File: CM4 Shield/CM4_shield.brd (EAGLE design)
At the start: 191.8 x 123.4 mm, 40 parts, among them J1 TERMINALBLOCK/TOYO/2PIN/5MMPI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, J3 RASPBERRYPI-40-PIN-GPIO_PTH_N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, X4 DOOR LOCK, X6 TOWER LIGHT

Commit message: Design updates
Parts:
- moved TP18 7.55 mm to (112.4, 5.84)
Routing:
- net DOOR_FEEDBACK: track 79.6 -> 81.5 mm
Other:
- board text added: "24V"
- board text added: "DOOR FEEDBACK"
- board text added: "DOOR LOCK"
- board text added: "GND"
- board text added: "MF_DOOR"
- board text added: "MF_TWRL_G"
- board text added: "MF_TWRL_R"
- board text added: "MF_TWRL_Y"
- board text added: "TWR_G"
- board text added: "TWR_R"
- board text added: "TWR_Y"
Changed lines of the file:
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@@
 <wire x1="90.932" y1="61.468" x2="28.194" y2="55.626" width="0.001" layer="51"/>
 <wire x1="27.94" y1="61.214" x2="90.932" y2="55.626" width="0.001" layer="51"/>
-<text x="111.387" y="-1.656" size="1.016" layer="21">24V INPUT</text>
+<text x="113.927" y="2.662" size="1.016" layer="21">24V INPUT</text>
 <text x="67.818" y="41.529" size="1.016" layer="21" rot="R180">5V DISPLAY</text>
 <wire x1="131" y1="-6" x2="131" y2="0" width="0.0762" layer="51"/>
@@
 <wire x1="113.792" y1="13.716" x2="110.49" y2="17.018" width="0.1524" layer="20" curve="90"/>
 <wire x1="110.49" y1="17.018" x2="106.934" y2="17.018" width="0.1524" layer="20"/>
+<text x="108.458" y="-10.16" size="0.6096" layer="27">GND</text>
+<text x="99.822" y="-0.508" size="0.6096" layer="27" rot="R90">GND</text>
+<text x="124.968" y="-4.318" size="0.6096" layer="27" rot="R180">GND</text>
+<text x="105.41" y="29.21" size="0.3048" layer="27" rot="R180">DOOR LOCK</text>
+<text x="112.268" y="3.81" size="0.6096" layer="27">24V</text>
+<text x="114.554" y="2.032" size="0.6096" layer="27">24V</text>
+<text x="119.38" y="2.032" size="0.6096" layer="27">GND</text>
+<text x="119.634" y="30.226" size="0.4064" layer="27">TWR_R</text>
+<text x="121.412" y="8.382" size="0.4064" layer="27" rot="R270">TWR_G</text>
+<text x="120.65" y="42.418" size="0.4064" layer="27">TWR_Y</text>
+<text x="110.236" y="39.116" size="0.4064" layer="27">MF_DOOR</text>
+<text x="99.314" y="-10.16" size="0.3048" layer="27">MF_TWRL_R</text>
+<text x="102.616" y="-10.16" size="0.3048" layer="27">MF_TWRL_Y</text>
+<text x="105.41" y="-10.16" size="0.3048" layer="27">MF_TWRL_G</text>
+<text x="110.744" y="6.604" size="0.3048" layer="27">DOOR FEEDBACK</text>
 </plain>
 <attributes>
@@
 <element name="TP16" library="SparkFun-Connectors" library_urn="urn:adsk.eagle:library:513" package="PAD.03X.05" package3d_urn="urn:adsk.eagle:package:38285/1" value="" x="104.202" y="28.03" smashed="yes"/>
 <element name="TP17" library="SparkFun-Connectors" library_urn="urn:adsk.eagle:library:513" package="PAD.03X.05" package3d_urn="urn:adsk.eagle:package:38285/1" value="" x="111.138" y="40.382" smashed="yes"/>
-<element name="TP18" library="SparkFun-Connectors" library_urn="urn:adsk.eagle:library:513" package="PAD.03X.05" package3d_urn="urn:adsk.eagle:package:38285/1" value="" x="109.868" y="-1.274" smashed="yes"/>
+<element name="TP18" library="SparkFun-Connectors" library_urn="urn:adsk.eagle:library:513" package="PAD.03X.05" package3d_urn="urn:adsk.eagle:package:38285/1" value="" x="112.408" y="5.838" smashed="yes"/>
 <element name="TP19" library="SparkFun-Connectors" library_urn="urn:adsk.eagle:library:513" package="PAD.03X.05" package3d_urn="urn:adsk.eagle:package:38285/1" value="" x="109.38" y="-8.98" smashed="yes"/>
 <element name="TP2" library="SparkFun-Connectors" library_urn="urn:adsk.eagle:library:513" package="PAD.03X.05" package3d_urn="urn:adsk.eagle:package:38285/1" value="" x="100.724" y="-9.148" smashed="yes"/>
@@
 <contactref element="X4" pad="3"/>
 <contactref element="J3" pad="37"/>
-<wire x1="109.252" y1="1.84" x2="109.868" y2="1.224" width="0.3048" layer="1"/>
-<wire x1="109.868" y1="1.224" x2="109.868" y2="-1.274" width="0.3048" layer="1"/>
+<wire x1="109.252" y1="1.84" x2="112.408" y2="4.996" width="0.3048" layer="1"/>
+<wire x1="112.408" y1="5.838" x2="112.408" y2="4.996" width="0.3048" layer="1"/>
 <wire x1="118.2243" y1="51.300384375" x2="120.106684375" y2="51.300384375" width="0.6096" layer="1"/>
 <wire x1="120.106684375" y1="51.300384375" x2="120.6223" y2="51.816" width="0.6096" layer="1"/>

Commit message: update to board design
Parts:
- removed FWLOGO_1: FWLOGO, FracktalWorks:FWLOGO
- removed J1: TERMINALBLOCK/TOYO/2PIN/5MMPITCH, FracktalWorks:TERMINALBLOCK/TOYO/2PIN/5MMPITCH
- added J4: 2828XX-2282837-2, Connector:TERMBLK_508-2N
- added TP3: (no value), SparkFun-Connectors:PAD.03X.05
- added X1: JST-XH-02-PIN-LONG-PAD, Rembrandt Electronics - JST XH Connectors v1-0:JST-XH-02-PACKAGE-LONG-PAD
- moved TP18 5.86 mm to (106.8, 7.62)
- moved TP12 5.79 mm to (119.5, -0.00)
- moved TP4 3.66 mm to (114.9, -0.00)
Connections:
- new net BUZZER: J3.32, TP3.P$1, X1.1
- net +24V: now also J4.1; no longer J1.1
- net GND: now also J4.2, X1.2; no longer J1.2
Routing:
- net BUZZER: track 0.00 -> 69.7 mm
- net MF_DOOR: track 51.5 -> 45.3 mm
- net GND: track 179.3 -> 174.0 mm, vias 6 -> 5
- net DOOR_FEEDBACK: track 81.5 -> 76.9 mm
- net +24V: track 141.5 -> 143.9 mm
- net MF_TWRL_R: track 62.3 -> 64.2 mm
- net MF_TWR_G: track 43.9 -> 45.3 mm
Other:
- outline, holes or cut-outs redrawn
- board text added: "+24V"
- board text added: "BUZZER"
- board text removed: "24V"
- board text removed: "5V DISPLAY"

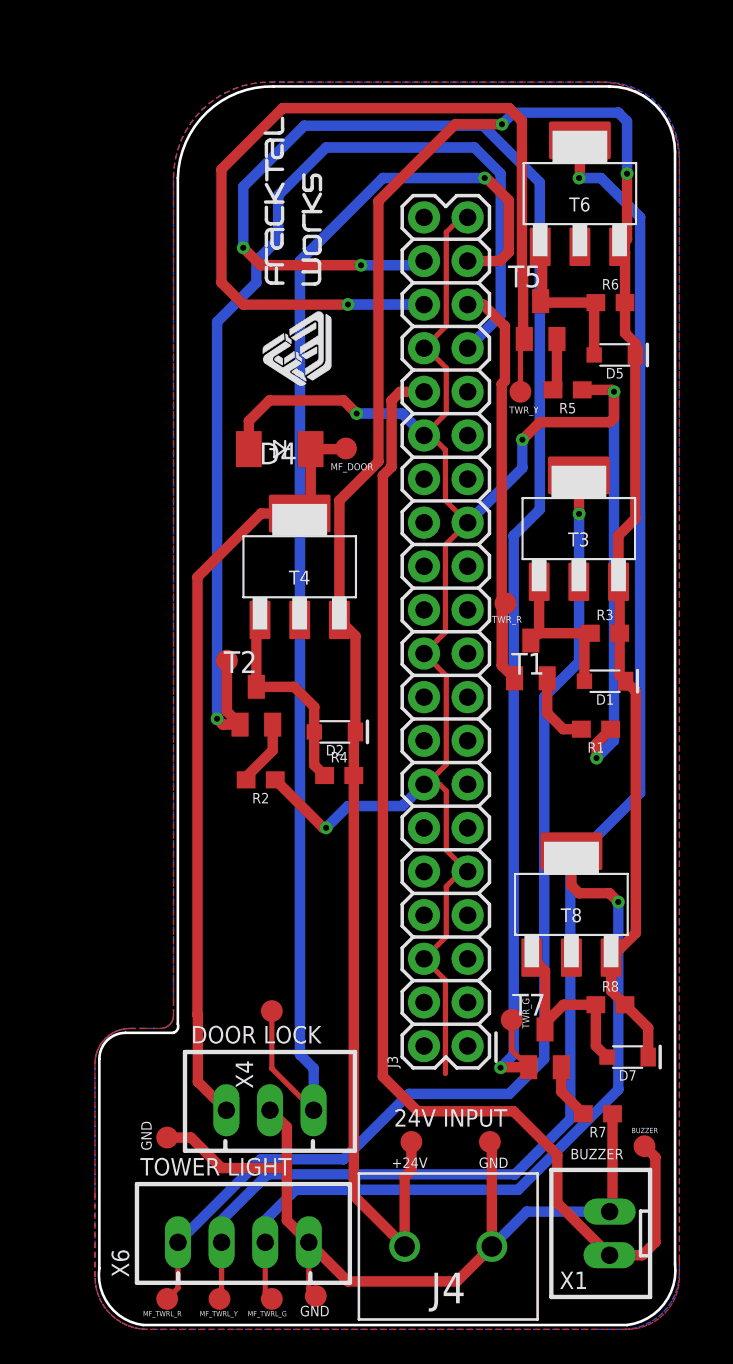
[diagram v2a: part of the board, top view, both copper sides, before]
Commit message: Correction of DRC check, and changes accordingly
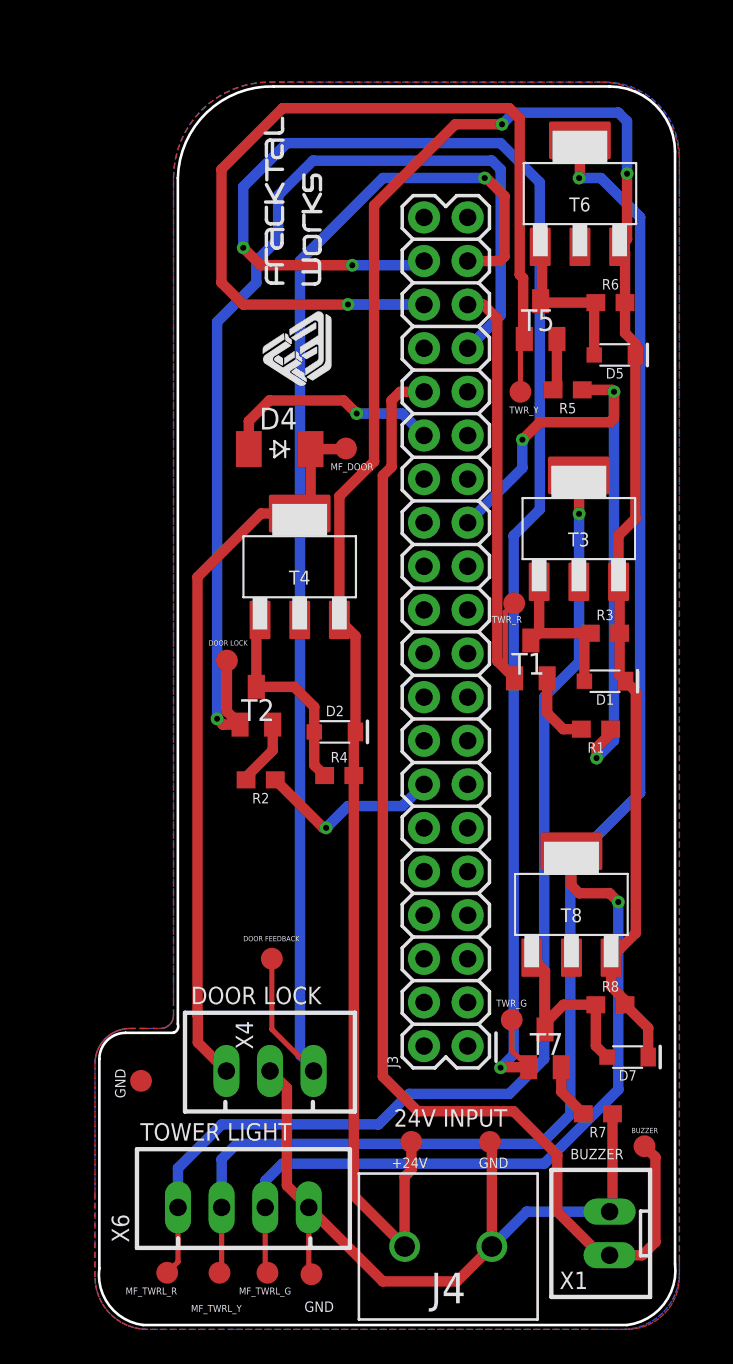
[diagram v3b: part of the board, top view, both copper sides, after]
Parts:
- moved TP13 3.64 mm to (99.2, 3.55)
- moved TP18 3.05 mm to (106.8, 10.7)
- moved X4 2.29 mm to (106.7, 4.13)
- moved X6 2.03 mm to (105.2, -3.82)
- moved TP10 1.55 mm to (106.6, -7.62)
- moved TP2 1.52 mm to (100.7, -7.62)
- moved TP6 1.52 mm to (103.8, -7.62)
- moved TP19 1.30 mm to (109.1, -7.71)
- moved TP1 0.51 mm to (120.9, 31.4)
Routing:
- net GND: track 174.0 -> 109.1 mm
- net MF_DOOR: track 45.3 -> 43.0 mm
- net DOOR_FEEDBACK: track 76.9 -> 75.2 mm
- net MF_TWRL_R: track 64.2 -> 65.2 mm
- net TWR_G: track 92.1 -> 91.2 mm
